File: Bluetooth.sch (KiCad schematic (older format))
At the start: 6 parts, among them P1 CONN_02X04, P2 CONN_01X06, P3 CONN_01X01

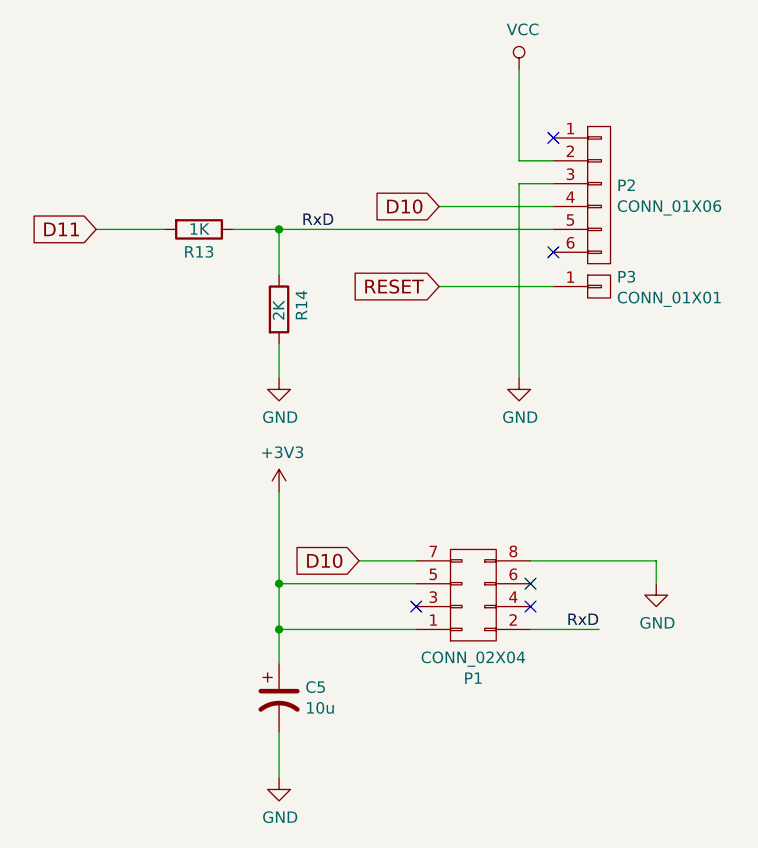
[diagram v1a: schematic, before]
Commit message: finalizada la ubicacion de componentes para la V0.4
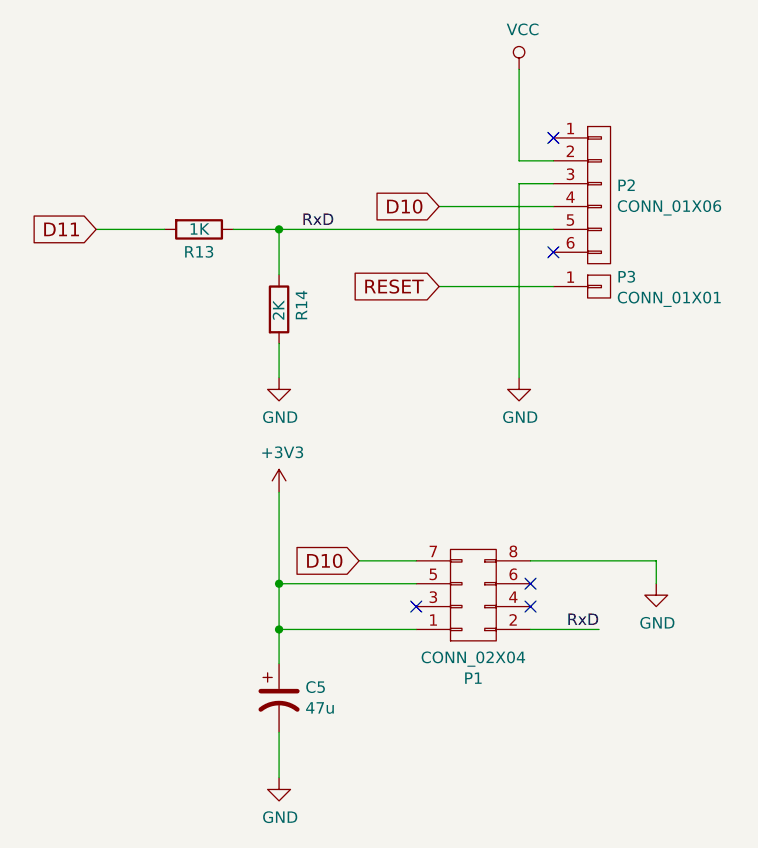
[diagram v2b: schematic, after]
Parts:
- C5: value 10u -> 47u; footprint Capacitors_Tantalum_SMD:Tantalum_Case-A_EIA-3216-18_Reflow -> Capacitors_SMD:C_1206; Fabricante avx -> murata; Ref TAJA106M010RNJ -> GRM31CR61A476ME15L; Ref_Proveedor TAJA106M010R -> GRM31CR61A476ME15L
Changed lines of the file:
@@
 P 2000 3800
 F 0 "C5" H 2115 3846 50  0000 L CNN
-F 1 "10u" H 2115 3755 50  0000 L CNN
-F 2 "Capacitors_Tantalum_SMD:Tantalum_Case-A_EIA-3216-18_Reflow" H 2000 3800 50  0001 C CNN
-F 3 "http://www.tme.eu/es/Document/85f84849ee9dc6997647a15c8c95a9d3/taj.pdf" H 2000 3800 50  0001 C CNN
-F 4 "avx" H 2000 3800 60  0001 C CNN "Fabricante"
-F 5 "TAJA106M010RNJ" H 2000 3800 60  0001 C CNN "Ref"
+F 1 "47u" H 2115 3755 50  0000 L CNN
+F 2 "Capacitors_SMD:C_1206" H 2000 3800 50  0001 C CNN
+F 3 "http://www.tme.eu/es/Document/e3e731e59cc68b1ab6d46b158bb05733/MURATA_GRM.pdf" H 2000 3800 50  0001 C CNN
+F 4 "murata" H 2000 3800 60  0001 C CNN "Fabricante"
+F 5 "GRM31CR61A476ME15L" H 2000 3800 60  0001 C CNN "Ref"
 F 6 "~" H 2000 3800 60  0001 C CNN "Potencia"
 F 7 "~" H 2000 3800 60  0001 C CNN "Tolerancia"
 F 8 "tme" H 2000 3800 60  0001 C CNN "Provedor"
-F 9 "TAJA106M010R" H 2000 3800 60  0001 C CNN "Ref_Proveedor"
+F 9 "GRM31CR61A476ME15L" H 2000 3800 60  0001 C CNN "Ref_Proveedor"
 	1    2000 3800
 	1    0    0    -1
